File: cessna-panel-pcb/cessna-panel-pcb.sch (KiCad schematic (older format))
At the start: 45 parts, among them J1 Conn_02x15_Odd_Even, SW1 SW_Push_DPDT, SW10 SW_SPDT, SW11 SW_Push_DPDT, SW12 SW_Push_DPDT, SW13 SW_SPDT, SW14 SW_Push_DPDT, SW15 SW_SPDT, SW16 Magneto rotary switch, SW17 SW_Push_DPDT, SW18 SW_SPDT, SW19 SW_SPDT, SW2 SW_Push_DPDT, SW20 SW_Push_DPDT, SW3 SW_SPDT, SW4 SW_SPDT, SW5 SW_SPDT, SW6 SW_SPDT, SW7 SW_Push_DPDT, SW8 SW_Push_DPDT, SW9 SW_SPDT

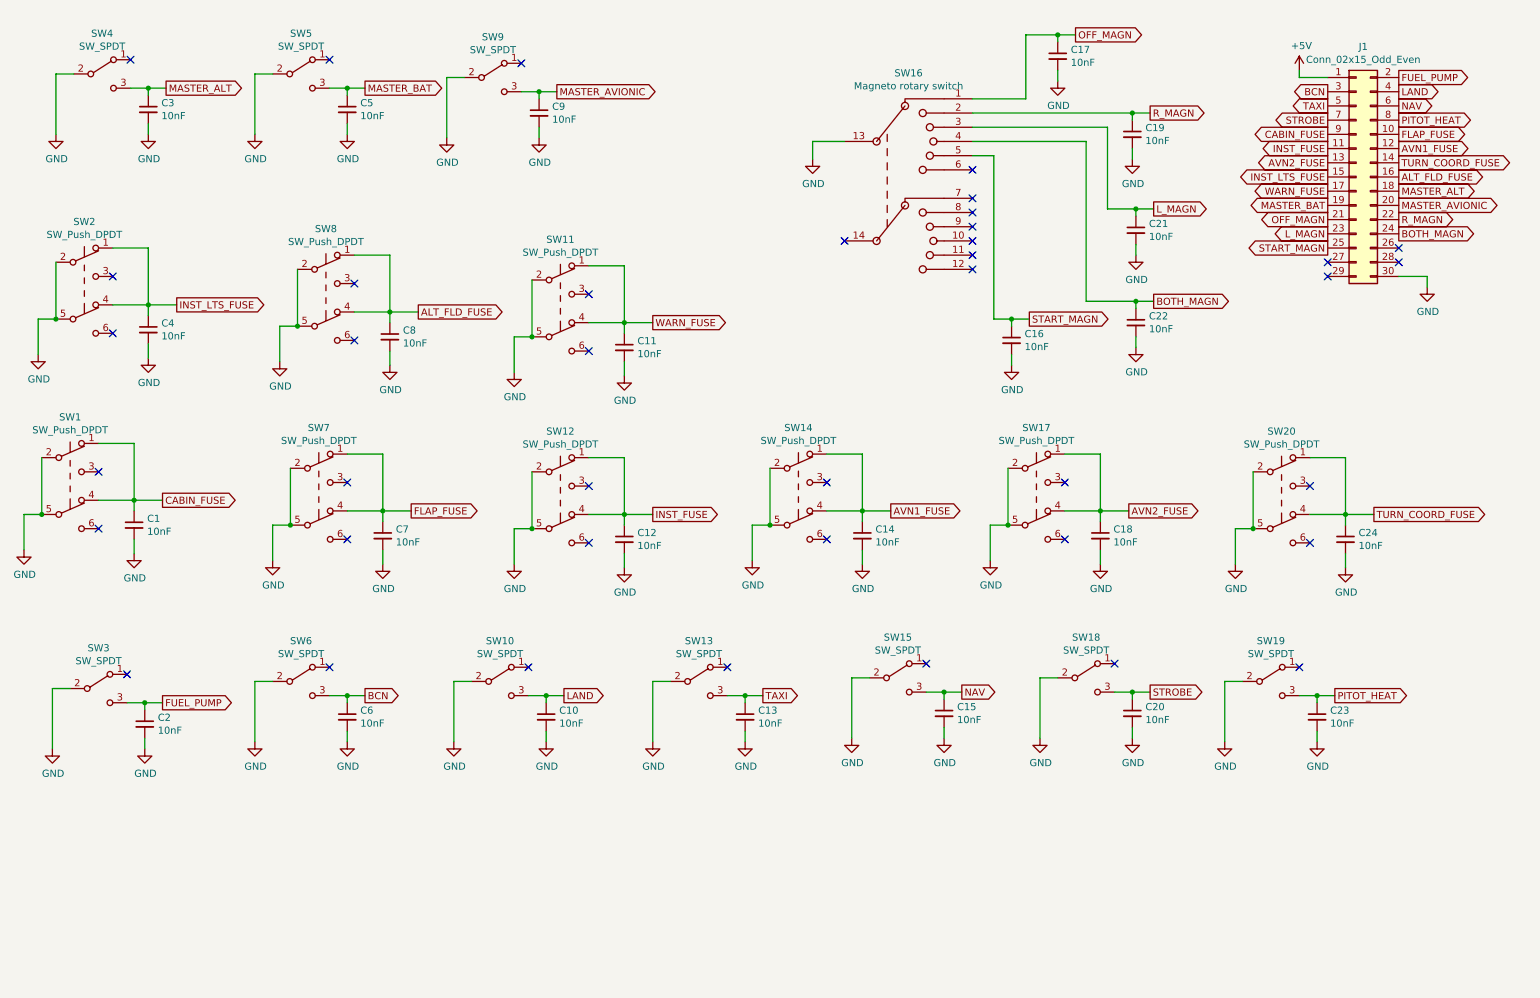
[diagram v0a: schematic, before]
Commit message: Diseño de PCb para conectar los Switches y los servos diseñada.
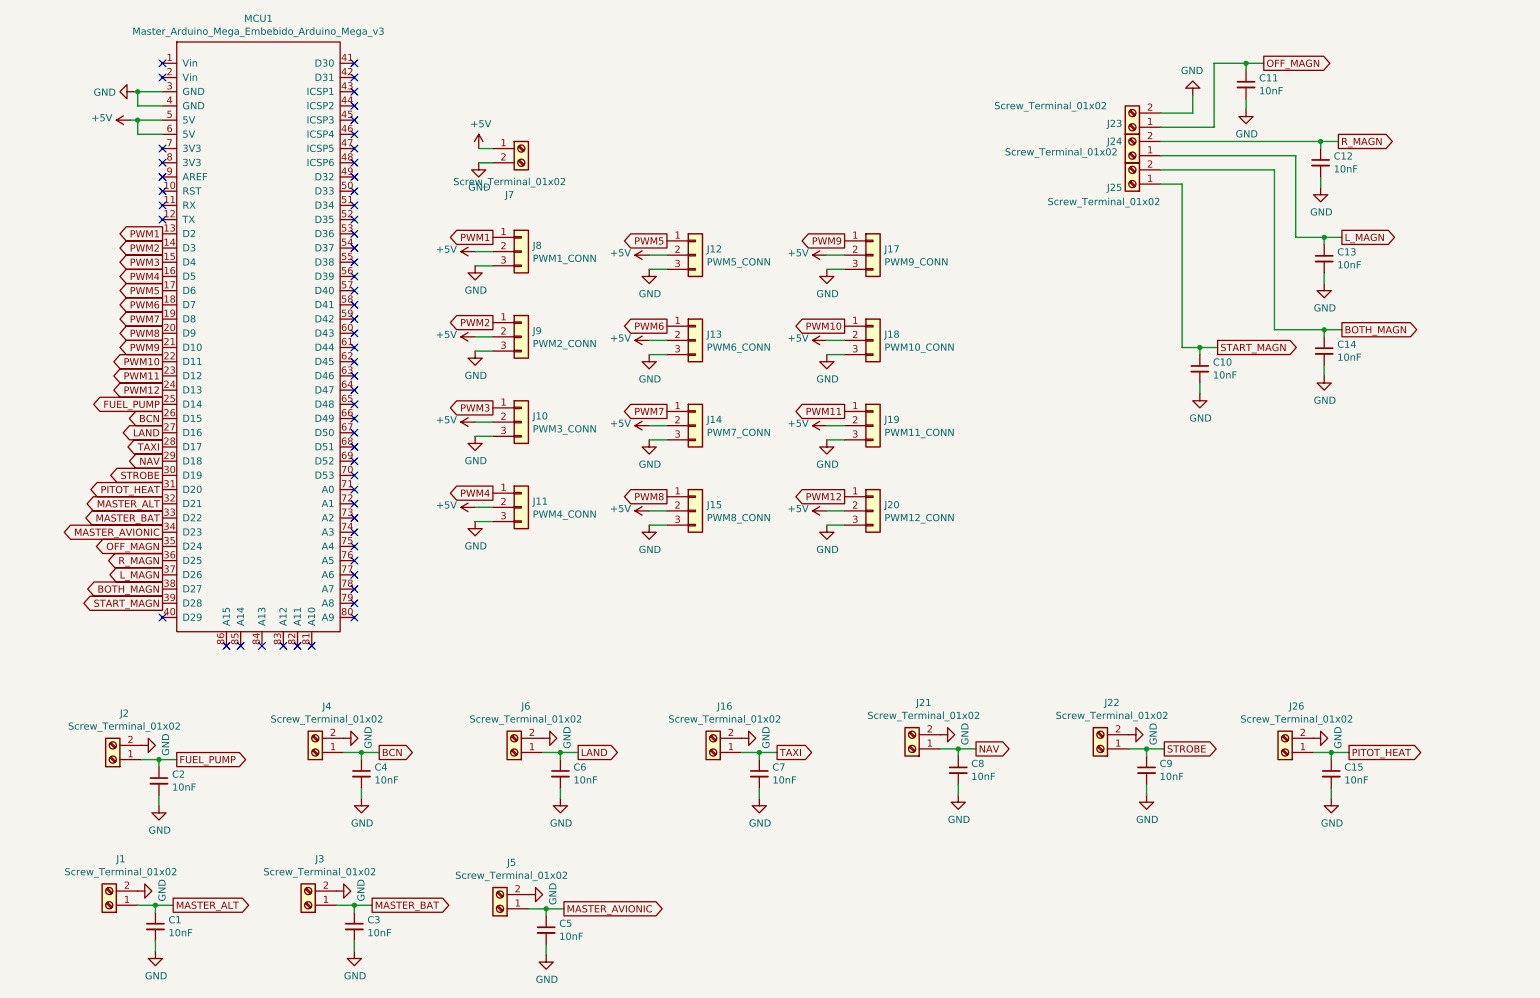
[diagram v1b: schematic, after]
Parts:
- removed C1, C11, C12, C14, C18, C24, C4, C7, C8: 10nF, symbol Device:C_Small
- removed J1: Conn_02x15_Odd_Even, symbol Connector_Generic:Conn_02x15_Odd_Even
- removed SW1, SW11, SW12, SW14, SW17, SW2, SW20, SW7, SW8: SW_Push_DPDT, symbol Switch:SW_Push_DPDT
- removed SW10, SW13, SW15, SW18, SW19, SW3, SW4, SW5, SW6, SW9: SW_SPDT, symbol Switch:SW_SPDT
- removed SW16: Magneto rotary switch, symbol Switch:SW_Rotary2x6
- added J1, J16, J2, J21, J22, J23, J24, J25, J26, J3, J4, J5, J6, J7: Screw_Terminal_01x02, TerminalBlock:TerminalBlock_bornier-2_P5.08mm, symbol Connector:Screw_Terminal_01x02
- added J10: PWM3_CONN, Connector_PinSocket_2.54mm:PinSocket_1x03_P2.54mm_Vertical, symbol Connector_Generic:Conn_01x03
- added J11: PWM4_CONN, Connector_PinSocket_2.54mm:PinSocket_1x03_P2.54mm_Vertical, symbol Connector_Generic:Conn_01x03
- added J12: PWM5_CONN, Connector_PinSocket_2.54mm:PinSocket_1x03_P2.54mm_Vertical, symbol Connector_Generic:Conn_01x03
- added J13: PWM6_CONN, Connector_PinSocket_2.54mm:PinSocket_1x03_P2.54mm_Vertical, symbol Connector_Generic:Conn_01x03
- added J14: PWM7_CONN, Connector_PinSocket_2.54mm:PinSocket_1x03_P2.54mm_Vertical, symbol Connector_Generic:Conn_01x03
- added J15: PWM8_CONN, Connector_PinSocket_2.54mm:PinSocket_1x03_P2.54mm_Vertical, symbol Connector_Generic:Conn_01x03
- added J17: PWM9_CONN, Connector_PinSocket_2.54mm:PinSocket_1x03_P2.54mm_Vertical, symbol Connector_Generic:Conn_01x03
- added J18: PWM10_CONN, Connector_PinSocket_2.54mm:PinSocket_1x03_P2.54mm_Vertical, symbol Connector_Generic:Conn_01x03
- added J19: PWM11_CONN, Connector_PinSocket_2.54mm:PinSocket_1x03_P2.54mm_Vertical, symbol Connector_Generic:Conn_01x03
- added J20: PWM12_CONN, Connector_PinSocket_2.54mm:PinSocket_1x03_P2.54mm_Vertical, symbol Connector_Generic:Conn_01x03
- added J8: PWM1_CONN, Connector_PinSocket_2.54mm:PinSocket_1x03_P2.54mm_Vertical, symbol Connector_Generic:Conn_01x03
- added J9: PWM2_CONN, Connector_PinSocket_2.54mm:PinSocket_1x03_P2.54mm_Vertical, symbol Connector_Generic:Conn_01x03
- added MCU1: Master_Arduino_Mega_Embebido_Arduino_Mega_v3, Mega2560-pro-mini-radio:MEGA_Embebido, symbol Master-cache:Master_Arduino_Mega_Embebido_Arduino_Mega_v3
- C1: renamed from C3; footprint (none) -> Capacitor_THT:C_Disc_D3.8mm_W2.6mm_P2.50mm
- C10: renamed from C16; footprint (none) -> Capacitor_THT:C_Disc_D3.8mm_W2.6mm_P2.50mm
- C11: renamed from C17; footprint (none) -> Capacitor_THT:C_Disc_D3.8mm_W2.6mm_P2.50mm
- C12: renamed from C19; footprint (none) -> Capacitor_THT:C_Disc_D3.8mm_W2.6mm_P2.50mm
- C13: renamed from C21; footprint (none) -> Capacitor_THT:C_Disc_D3.8mm_W2.6mm_P2.50mm
- C14: renamed from C22; footprint (none) -> Capacitor_THT:C_Disc_D3.8mm_W2.6mm_P2.50mm
- C15: renamed from C23; footprint (none) -> Capacitor_THT:C_Disc_D3.8mm_W2.6mm_P2.50mm
- C2: footprint (none) -> Capacitor_THT:C_Disc_D3.8mm_W2.6mm_P2.50mm
- C3: renamed from C5; footprint (none) -> Capacitor_THT:C_Disc_D3.8mm_W2.6mm_P2.50mm
- C4: renamed from C6; footprint (none) -> Capacitor_THT:C_Disc_D3.8mm_W2.6mm_P2.50mm
- C5: renamed from C9; footprint (none) -> Capacitor_THT:C_Disc_D3.8mm_W2.6mm_P2.50mm
- C6: renamed from C10; footprint (none) -> Capacitor_THT:C_Disc_D3.8mm_W2.6mm_P2.50mm
- C7: renamed from C13; footprint (none) -> Capacitor_THT:C_Disc_D3.8mm_W2.6mm_P2.50mm
- C8: renamed from C15; footprint (none) -> Capacitor_THT:C_Disc_D3.8mm_W2.6mm_P2.50mm
- C9: renamed from C20; footprint (none) -> Capacitor_THT:C_Disc_D3.8mm_W2.6mm_P2.50mm
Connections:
- net +5V: now also J10.2 (Pin_2), J11.2 (Pin_2), J12.2 (Pin_2), J13.2 (Pin_2), J14.2 (Pin_2), J15.2 (Pin_2), J17.2 (Pin_2), J18.2 (Pin_2), J19.2 (Pin_2), J20.2 (Pin_2), J7.1 (Pin_1), J8.2 (Pin_2), J9.2 (Pin_2), MCU1.5 (5V), MCU1.6 (5V)
- net BCN: now also J4.1 (Pin_1), MCU1.26 (D15)
- net BOTH_MAGN: now also J25.2 (Pin_2), MCU1.38 (D27)
- net FUEL_PUMP: now also J2.1 (Pin_1), MCU1.25 (D14)
- net GND: now also J1.2 (Pin_2), J10.3 (Pin_3), J11.3 (Pin_3), J12.3 (Pin_3), J13.3 (Pin_3), J14.3 (Pin_3), J15.3 (Pin_3), J16.2 (Pin_2), J17.3 (Pin_3), J18.3 (Pin_3), J19.3 (Pin_3), J2.2 (Pin_2), J20.3 (Pin_3), J21.2 (Pin_2), J22.2 (Pin_2), J23.2 (Pin_2), J26.2 (Pin_2), J3.2 (Pin_2), J4.2 (Pin_2), J5.2 (Pin_2), J6.2 (Pin_2), J7.2 (Pin_2), J8.3 (Pin_3), J9.3 (Pin_3), MCU1.3 (GND), MCU1.4 (GND)
- net LAND: now also J6.1 (Pin_1), MCU1.27 (D16)
- net L_MAGN: now also J24.1 (Pin_1), MCU1.37 (D26)
- net MASTER_ALT: now also J1.1 (Pin_1), MCU1.32 (D21)
- net MASTER_AVIONIC: now also J5.1 (Pin_1), MCU1.34 (D23)
- net MASTER_BAT: now also J3.1 (Pin_1), MCU1.33 (D22)
- net NAV: now also J21.1 (Pin_1), MCU1.29 (D18)
- net OFF_MAGN: now also J23.1 (Pin_1), MCU1.35 (D24)
- net PITOT_HEAT: now also J26.1 (Pin_1), MCU1.31 (D20)
- net R_MAGN: now also J24.2 (Pin_2), MCU1.36 (D25)
- net START_MAGN: now also J25.1 (Pin_1), MCU1.39 (D28)
- net STROBE: now also J22.1 (Pin_1), MCU1.30 (D19)
- net TAXI: now also J16.1 (Pin_1), MCU1.28 (D17)
- new net PWM1: J8.1 (Pin_1), MCU1.13 (D2)
- new net PWM10: J18.1 (Pin_1), MCU1.22 (D11)
- new net PWM11: J19.1 (Pin_1), MCU1.23 (D12)
- new net PWM12: J20.1 (Pin_1), MCU1.24 (D13)
- new net PWM2: J9.1 (Pin_1), MCU1.14 (D3)
- new net PWM3: J10.1 (Pin_1), MCU1.15 (D4)
- new net PWM4: J11.1 (Pin_1), MCU1.16 (D5)
- new net PWM5: J12.1 (Pin_1), MCU1.17 (D6)
- new net PWM6: J13.1 (Pin_1), MCU1.18 (D7)
- new net PWM7: J14.1 (Pin_1), MCU1.19 (D8)
- new net PWM8: J15.1 (Pin_1), MCU1.20 (D9)
- new net PWM9: J17.1 (Pin_1), MCU1.21 (D10)
- no-connect marks 40 -> 55
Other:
- moved on the sheet: C1, C10, C11, C12, C13, C14, C15, C2, C3, C4, C5, C6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
